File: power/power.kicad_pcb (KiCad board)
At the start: 2 copper layers, 100 x 100 mm, 34 parts, among them K1 MASTER_LIVE, K2 PREHEAT, M3_MOUNT VAL**, P1 CONTROL, P2 MAINS_INLET, P3 LOAD_OUTLET, Q1 BC817-40, Q2 BC817-40, U1 VTX214, U2 ACS710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

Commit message: Lots of footprint modifications
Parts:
- added D1: POWER, power:LED-0805, F.Cu at (66.8, 126.7)
- P2: footprint power:GSP1_9103 -> power:GSP1_9103_no_protrude
- P3: footprint power:5001 -> power:5001_no_protrude
- R7: value 75R -> 300R
- R9: value 220R -> 300R
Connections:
- net V_OFFSET renamed Net-(C1-Pad1)
- D2 pad 1: Net-(D2-Pad1) -> +5V
- D2 pad 2: GND -> Net-(D2-Pad2)
- D3 pad 1: Net-(D3-Pad1) -> +5V
- D3 pad 2: GND -> Net-(D3-Pad2)
- K1 pad 1: GND -> Net-(K1-Pad1)
- K1 pad 2: Net-(K1-Pad2) -> +5V
- K2 pad 1: GND -> Net-(K2-Pad1)
- K2 pad 2: Net-(K2-Pad2) -> +5V
- Q1 pad 2: Net-(K1-Pad2) -> GND
- Q1 pad 3: +5V -> Net-(K1-Pad1)
- Q2 pad 2: Net-(K2-Pad2) -> GND
- Q2 pad 3: +5V -> Net-(K2-Pad1)
- R2 pad 1: Net-(D2-Pad1) -> Net-(K1-Pad1)
- R2 pad 2: Net-(K1-Pad2) -> Net-(D2-Pad2)
- R5 pad 1: Net-(D3-Pad1) -> Net-(K2-Pad1)
- R5 pad 2: Net-(K2-Pad2) -> Net-(D3-Pad2)
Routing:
- net Net-(K2-Pad2): track 14.8 -> 0.00 mm
- net GND: track 48.4 -> 61.9 mm, vias 11 -> 9
- net Net-(K1-Pad2): track 12.3 -> 0.00 mm
- net +5V: track 151.7 -> 157.1 mm
- net Net-(K1-Pad1): track 0.00 -> 4.68 mm
- net Net-(K2-Pad1): track 0.00 -> 3.46 mm
- net Net-(D2-Pad2): track 0.00 -> 2.92 mm, vias 0 -> 1
- net Net-(D2-Pad1): track 2.73 -> 0.00 mm
- net Net-(D3-Pad1): track 2.60 -> 0.00 mm
- net Net-(D3-Pad2): track 0.00 -> 2.39 mm, vias 0 -> 1

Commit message: Test points, rerouted relay drivers.
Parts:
- added P4: +5V, Connect:1pin, F.Cu at (46.8, 127.4)
- added P5: GND, Connect:1pin, F.Cu at (54.1, 127.4)
- added P6: I_SENSE, Connect:1pin, F.Cu at (81.4, 121.0)
- moved Q2 8.57 mm to (108.6, 122.2), turned to 180 degrees
- moved Q1 6.31 mm to (92.3, 122.0), turned to 180 degrees
- moved D3 5.84 mm to (114.0, 125.3)
- moved R5 5.84 mm to (114.0, 123.1)
- moved D2 5.74 mm to (97.0, 124.6)
- moved R2 5.72 mm to (97.0, 122.3)
- moved R4 5.18 mm to (108.6, 126.5), turned to 180 degrees
- moved R1 3.87 mm to (92.3, 126.0), turned to 180 degrees
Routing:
- net +5V: track 157.1 -> 170.9 mm
- net PREHEAT_RELAY: track 37.4 -> 30.2 mm
- net MASTER_RELAY: track 14.3 -> 8.31 mm
- net Net-(K2-Pad1): track 3.46 -> 8.63 mm
- net Net-(K1-Pad1): track 4.68 -> 9.74 mm
- net GND: track 61.9 -> 56.9 mm, vias 9 -> 10
- net I_SENSE: track 17.8 -> 20.5 mm
- net Net-(Q2-Pad1): track 3.13 -> 2.32 mm
- net Net-(D2-Pad2): track 2.92 -> 2.31 mm, vias 1 -> 0
- net Net-(Q1-Pad1): track 2.49 -> 1.94 mm
- net Net-(D3-Pad2): track 2.39 -> 2.31 mm, vias 1 -> 0

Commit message: Silk, cleanup, masking, gerbils
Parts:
- F1: value 100mA -> 100mA 5x20mm
- F2: value 13A -> 13A BS1362
- I SENSE: renamed from P6
- U4: value MOC3163-M -> MOC3163M
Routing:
- net GND: track 56.9 -> 119.3 mm
- net TRIAC_MAINS: track 76.4 -> 104.5 mm
- net /EARTH: track 78.1 -> 66.3 mm
- net LOAD_LIVE: track 65.1 -> 76.8 mm
- net MAINS_NEUTRAL: track 113.4 -> 105.4 mm
- net MAINS_LIVE: track 80.6 -> 75.0 mm
- net +5V: track 170.9 -> 171.7 mm
- net LOAD_NEUTRAL: track 98.4 -> 98.9 mm
- added copper zone on B.Cu, net LOAD_LIVE
- added copper zone on F.Cu, net LOAD_NEUTRAL
- added copper zone on F.Cu, net MAINS_NEUTRAL
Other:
- board text added: "2015-03-30 REVISION 1"
- board text added: "BTA16- 800BRG"
- board text added: "CURRENT SENSE"
- board text added: "MASTER RELAY"
- board text added: "POWER BOARD"
- board text added: "POWER BOARD DAVID TURNER ADAM GREIG JON SOWMAN"
- board text added: "PREHEAT RELAY"
- board text added: "SUPERVIDE"
- board text added: "THERMAL SWITCH"
- board text added: "VTX-214-003-105"

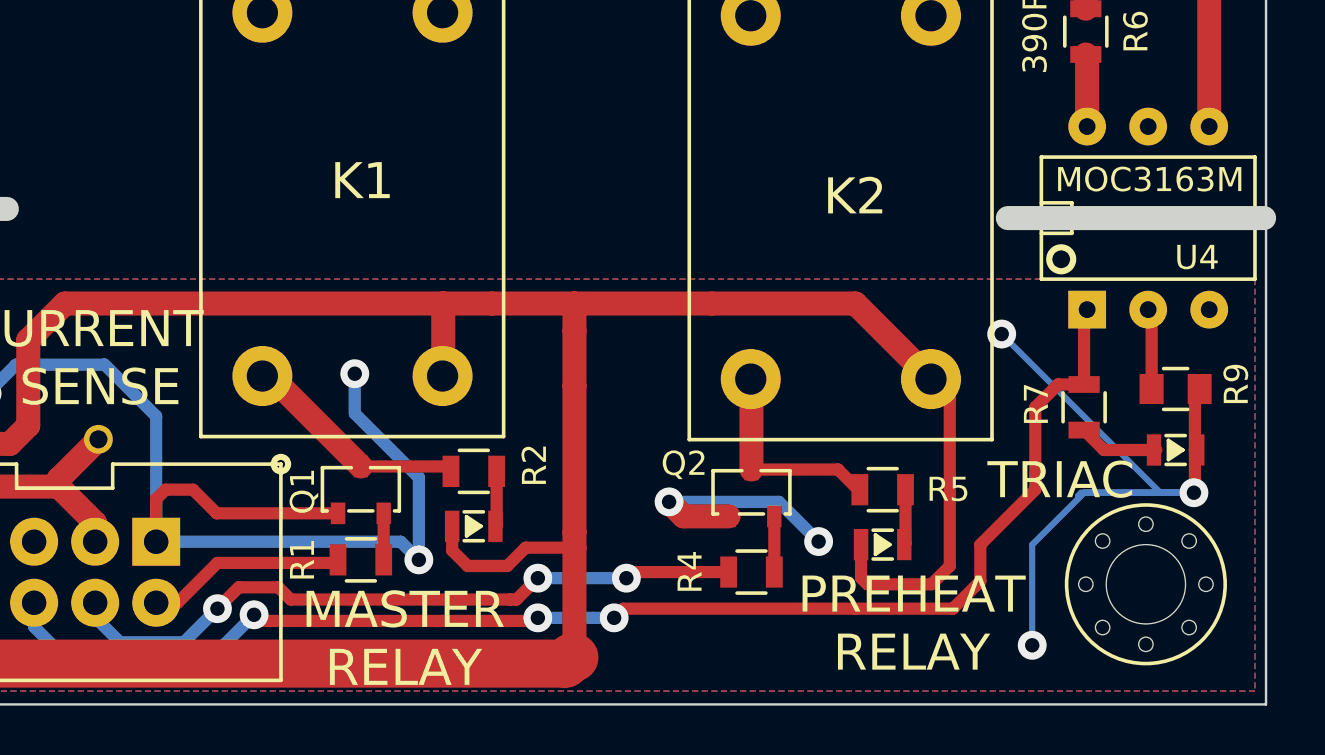
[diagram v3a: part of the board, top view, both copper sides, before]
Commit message: Power: Added relay flyback diodes.  Fixes #10
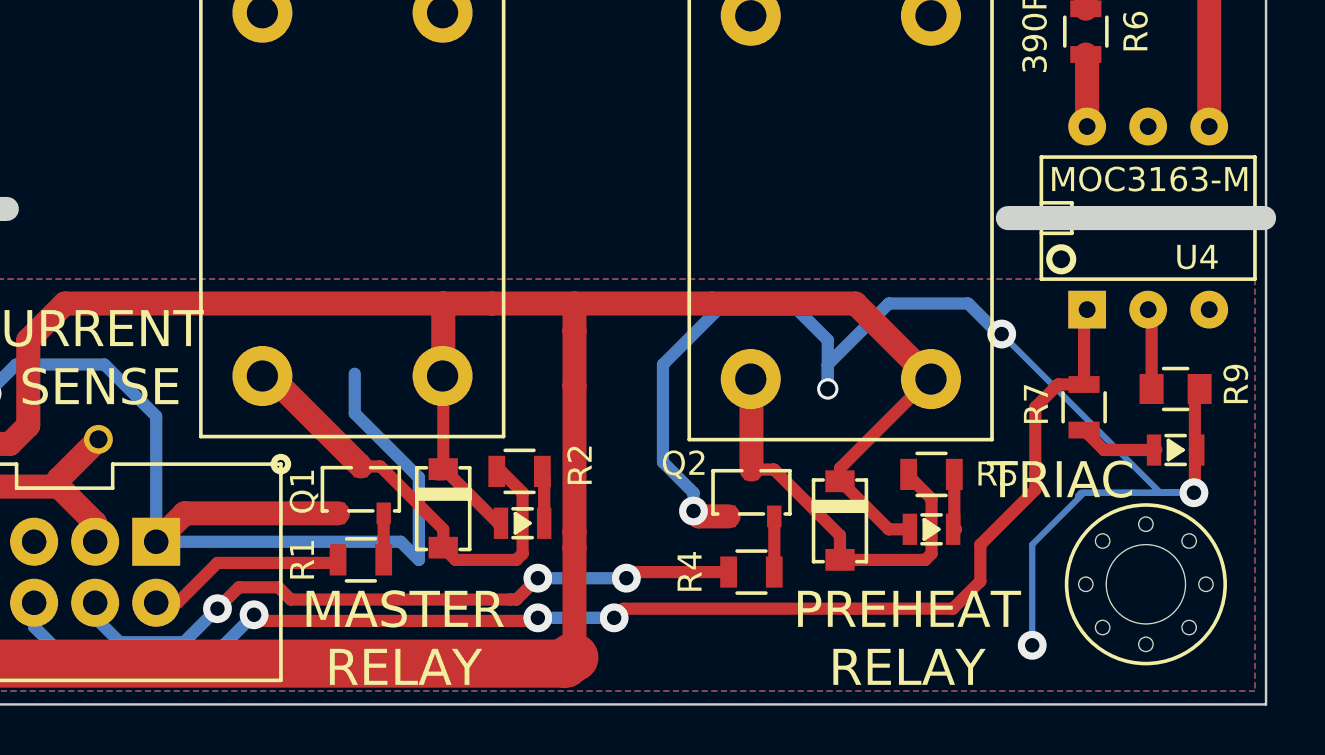
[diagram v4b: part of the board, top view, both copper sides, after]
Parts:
- added D5: MBR2H200SFT1G, power:SOD-123FL, F.Cu at (95.8, 124.0)
- added D6: MBR2H200SFT1G, power:SOD-123FL, F.Cu at (112.3, 124.5)
- F1: value 100mA 5x20mm -> 100mA
- F2: value 13A BS1362 -> 13A
- P6: renamed from I SENSE
- U4: value MOC3163M -> MOC3163-M
- moved D3 2.13 mm to (116.1, 124.7)
- moved R5 2.13 mm to (116.1, 122.4)
- moved D2 2.04 mm to (99.1, 124.5)
- moved R2 1.91 mm to (98.9, 122.3)
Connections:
- P1 pad 5: Net-(P1-Pad5) -> (no net)
- P1 pad 7: Net-(P1-Pad7) -> (no net)
- U2 pad 13: Net-(U2-Pad13) -> (no net)
- U2 pad 15: Net-(U2-Pad15) -> (no net)
- U4 pad 3: Net-(U4-Pad3) -> (no net)
- U4 pad 5: Net-(U4-Pad5) -> (no net)
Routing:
- net GND: track 119.3 -> 136.5 mm, vias 10 -> 8
- net Net-(D5-Pad2): track 9.74 -> 18.8 mm
- net Net-(D6-Pad2): track 8.63 -> 17.3 mm
- net +5V: track 171.7 -> 168.6 mm

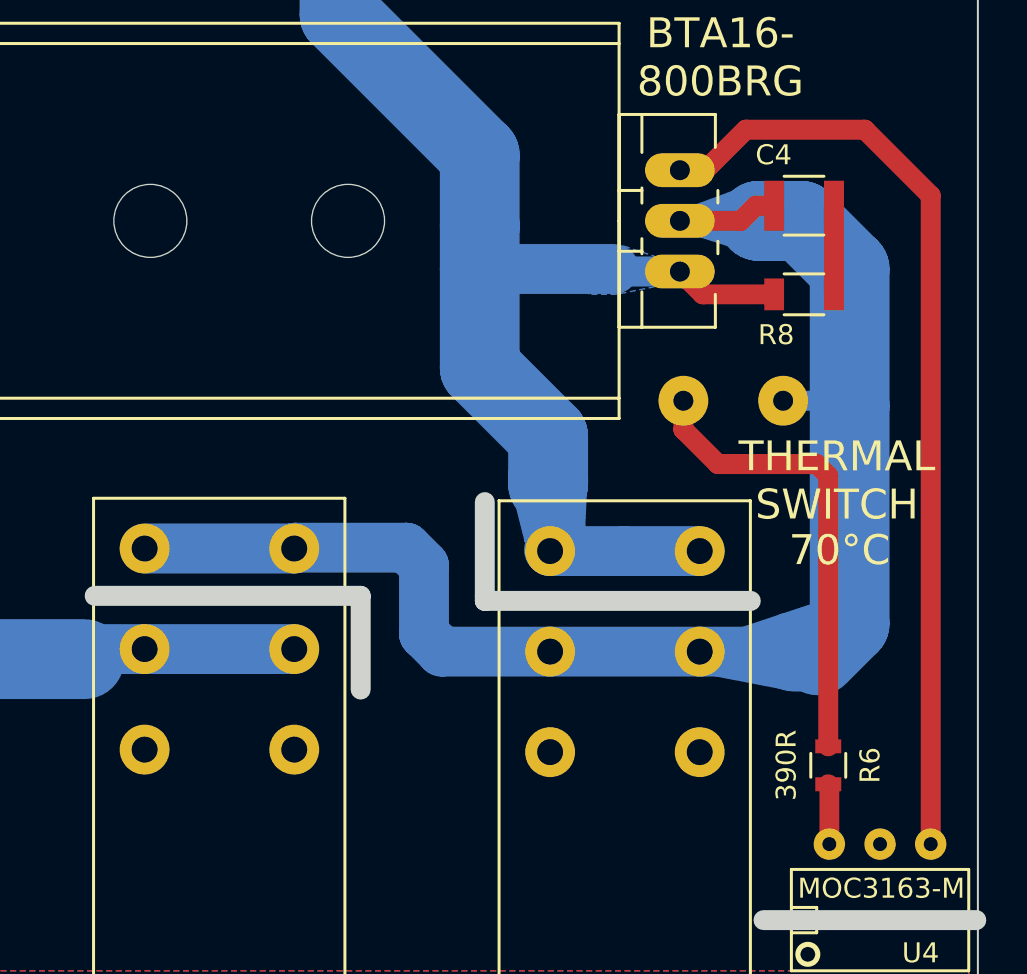
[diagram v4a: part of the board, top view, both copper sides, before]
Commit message: Power: Triac pin spacing, removed extra relay pads
Resolves #3
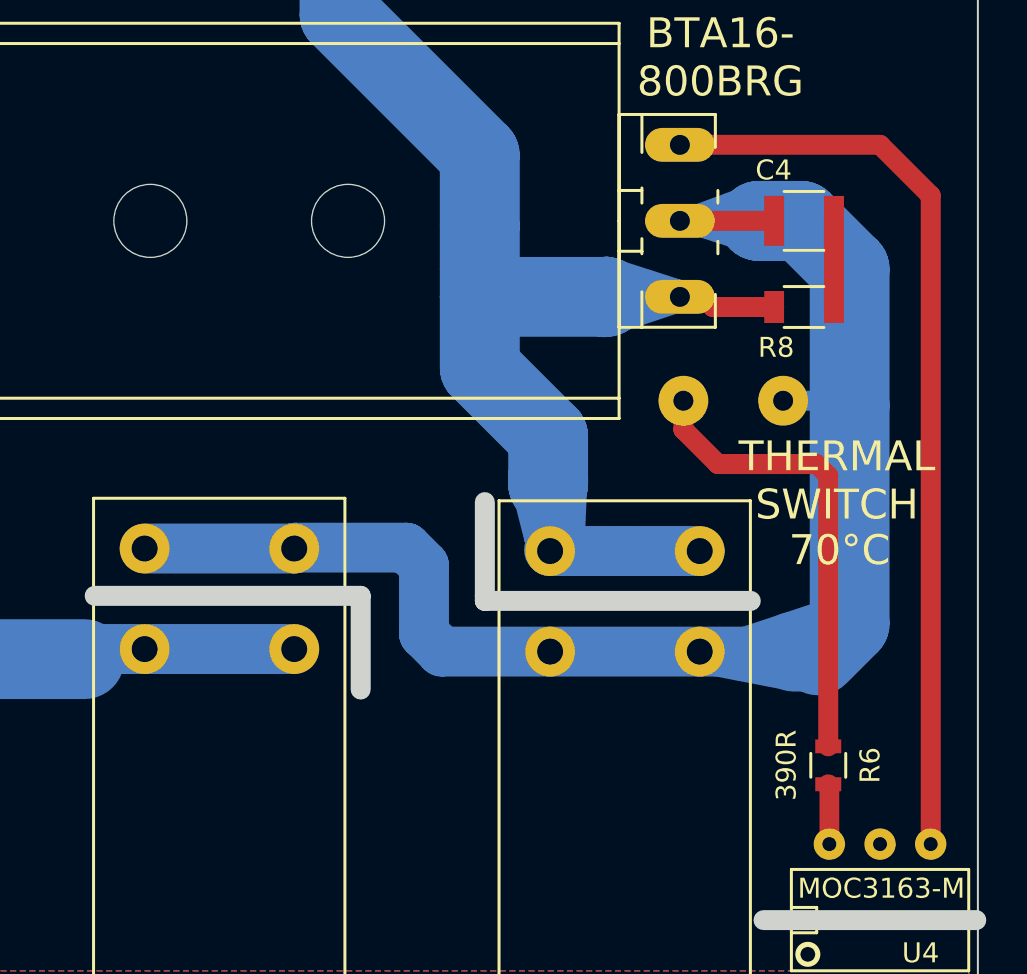
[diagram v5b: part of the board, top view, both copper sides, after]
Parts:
- moved C4 0.76 mm to (121.3, 76.7)
- moved R8 0.63 mm to (121.3, 81.0)
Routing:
- net LOAD_LIVE: track 76.8 -> 83.4 mm
- net Net-(U4-Pad4): track 47.3 -> 46.1 mm
- removed copper zone on B.Cu, net LOAD_LIVE

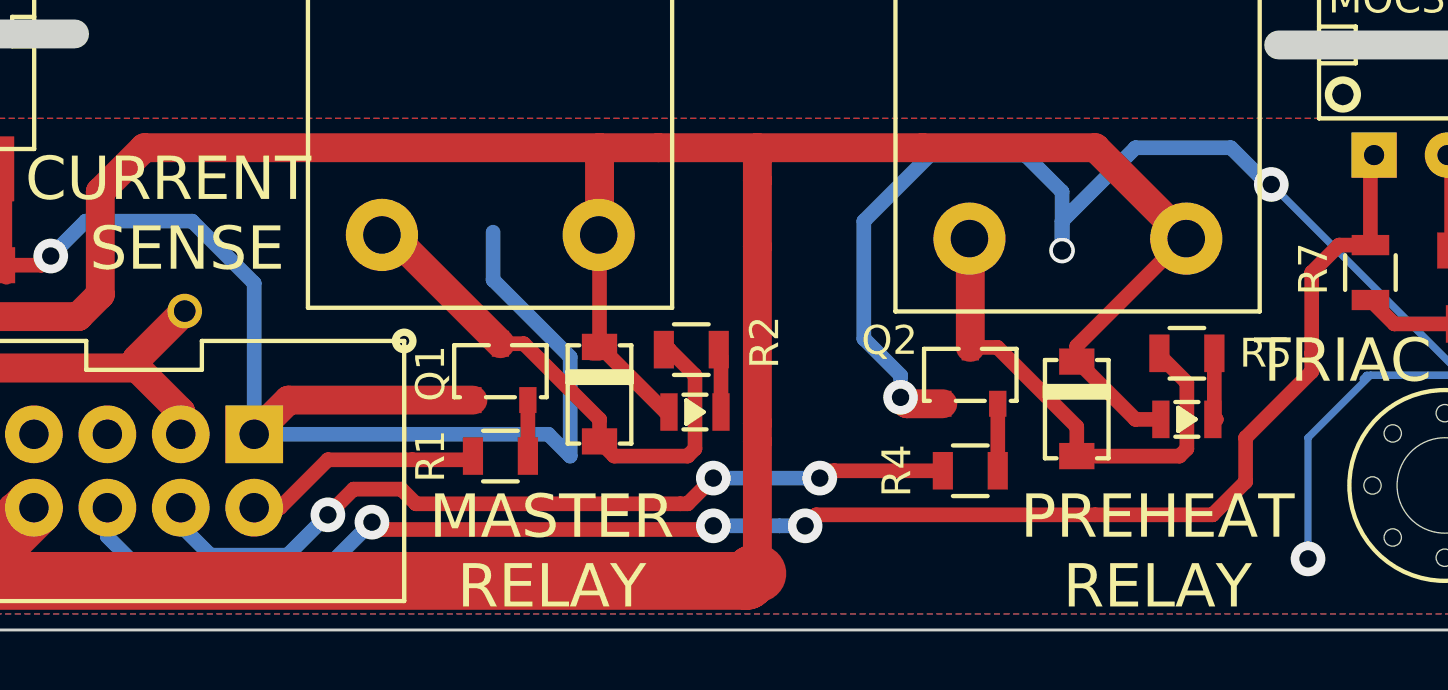
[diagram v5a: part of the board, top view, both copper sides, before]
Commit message: Flipped SOT23 footprint. Fixes #1
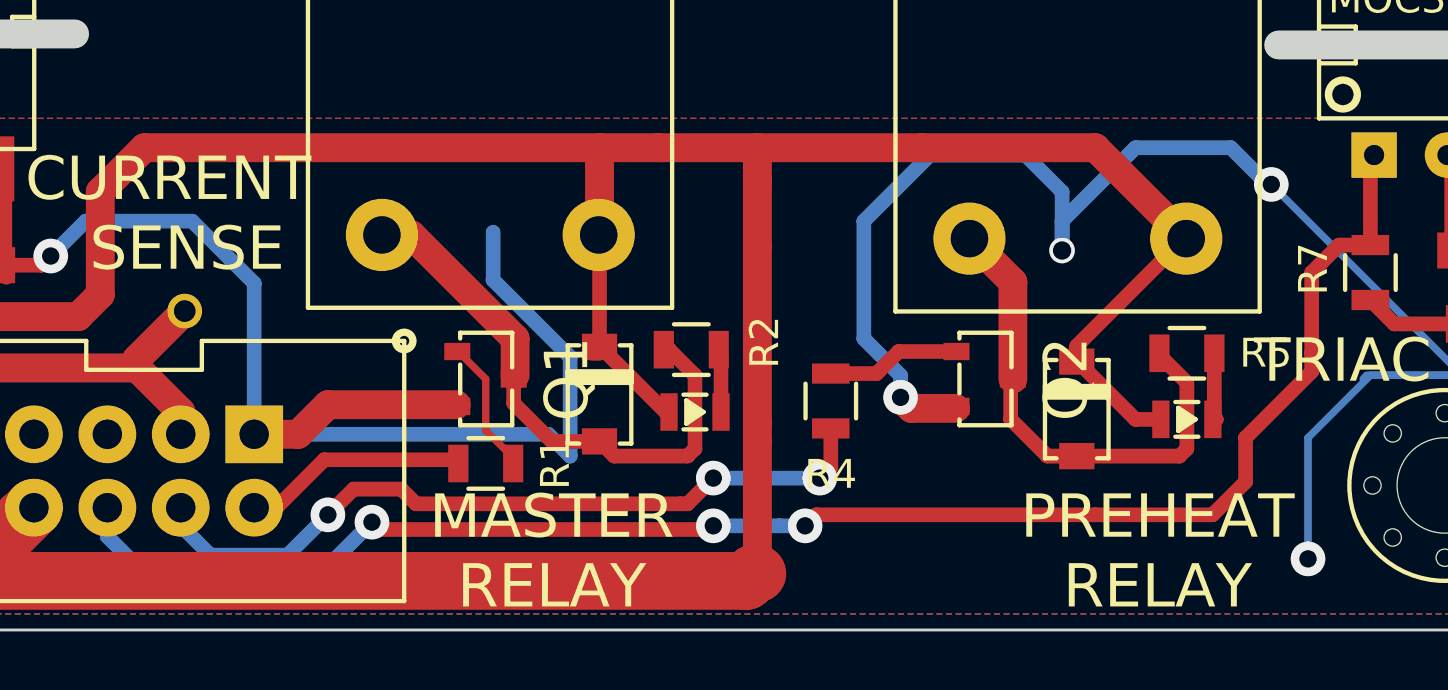
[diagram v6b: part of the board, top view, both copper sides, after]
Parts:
- moved R4 5.40 mm to (103.8, 124.1), turned to 270 degrees
- moved Q2 1.90 mm to (110.1, 123.3), turned to 90 degrees
- moved Q1 1.37 mm to (92.8, 123.3), turned to 90 degrees
- moved R1 0.57 mm to (91.8, 126.2)
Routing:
- net Net-(Q1-Pad1): track 1.94 -> 4.74 mm
- net PREHEAT_RELAY: track 29.9 -> 27.5 mm
- net Net-(Q2-Pad1): track 2.32 -> 4.67 mm
- net Net-(D5-Pad2): track 18.8 -> 19.7 mm
